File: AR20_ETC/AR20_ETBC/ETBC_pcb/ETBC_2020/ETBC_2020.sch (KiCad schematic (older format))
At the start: 3 parts

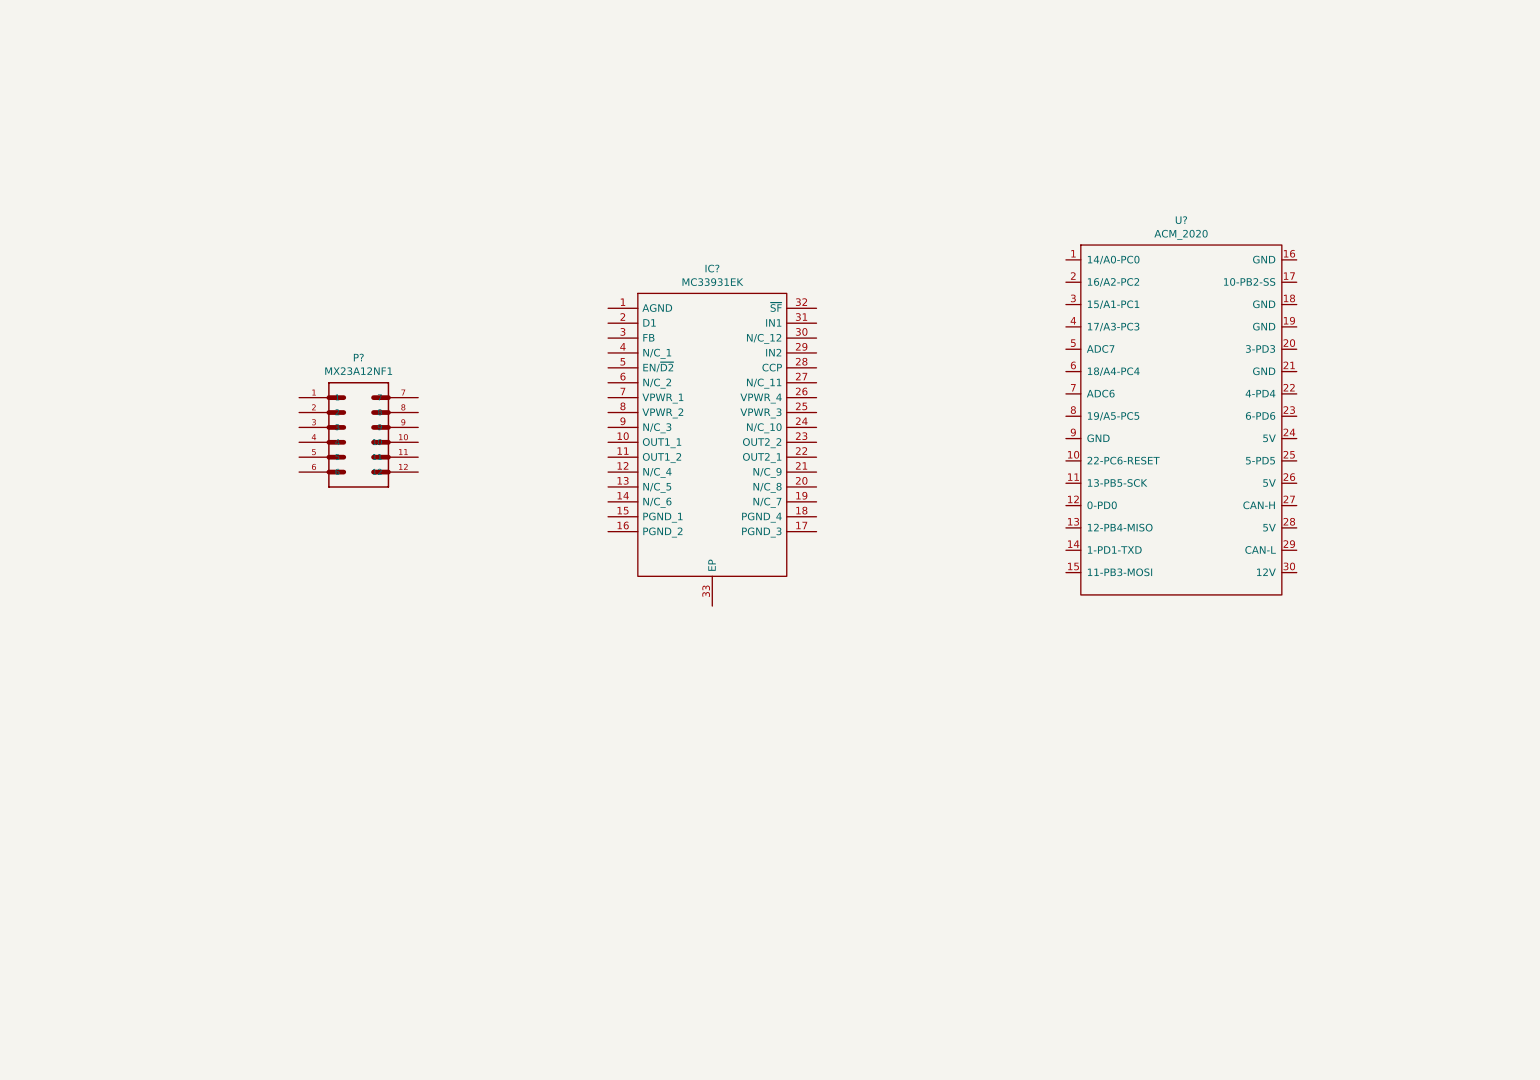
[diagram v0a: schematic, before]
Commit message: Shematic
Added leds
Added small components
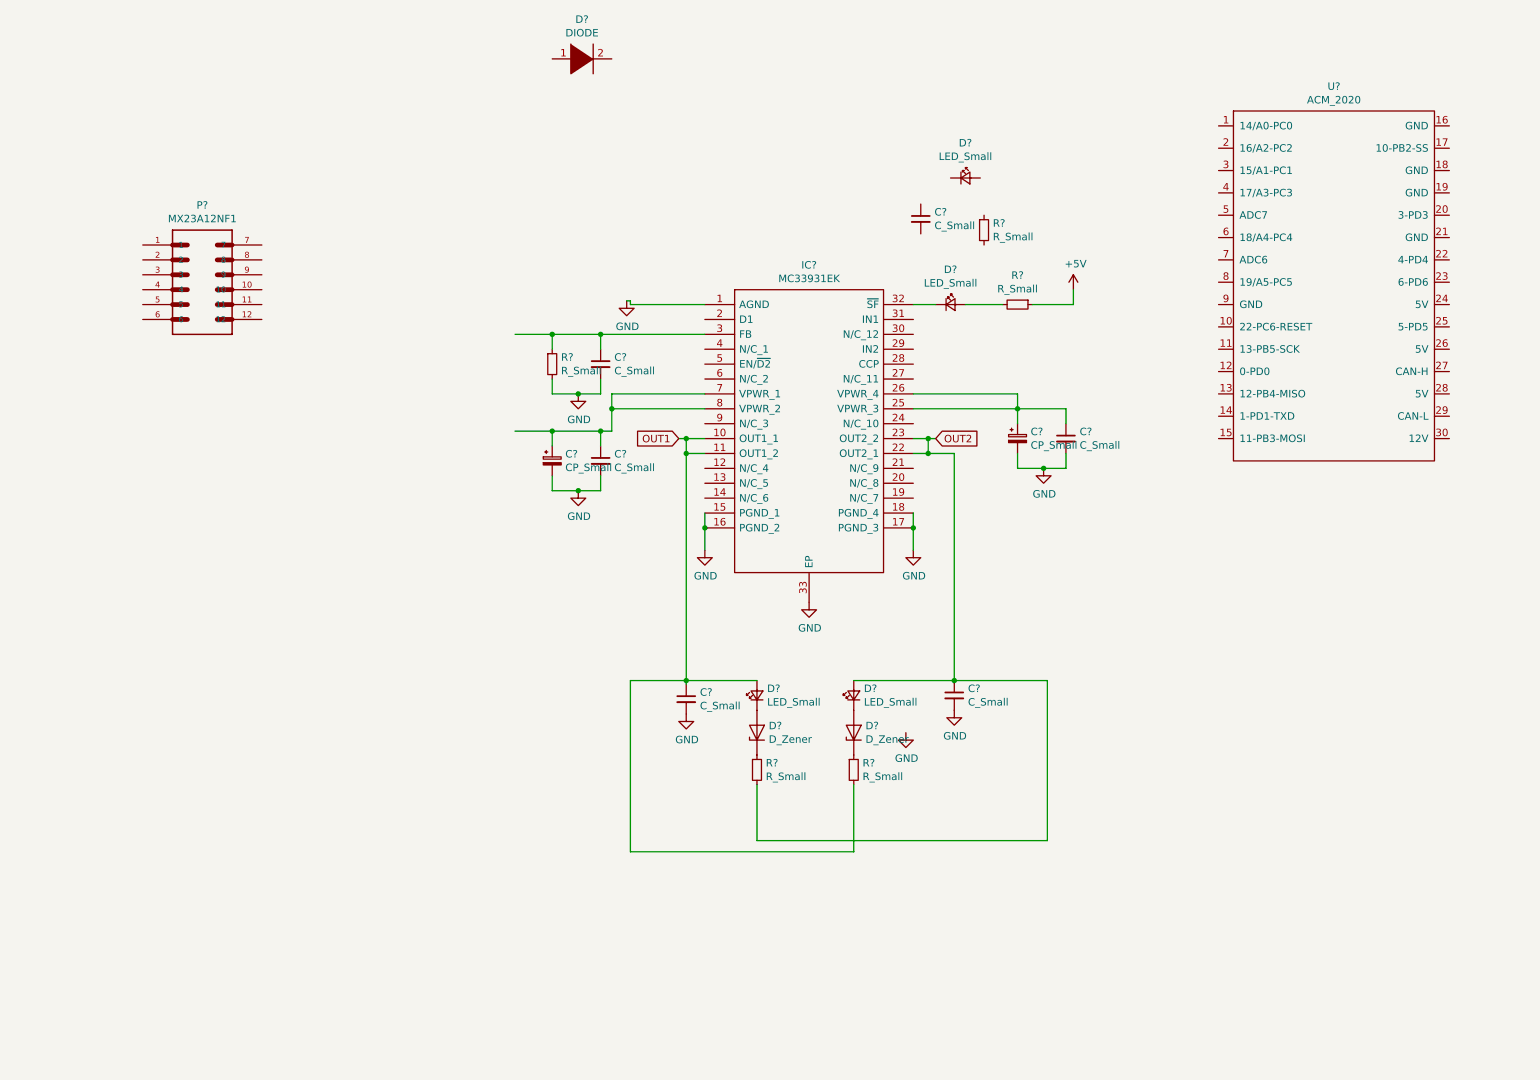
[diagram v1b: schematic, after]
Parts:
- added C? (x6): C_Small, symbol Device:C_Small
- added C? (x2): CP_Small, symbol Device:CP_Small
- added D? (x2): D_Zener, symbol Device:D_Zener
- added D?: DIODE, symbol pspice:DIODE
- added D? (x4): LED_Small, symbol Device:LED_Small
- added R? (x5): R_Small, symbol Device:R_Small
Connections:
- net labels added: +5V, GND, OUT1, OUT2
- wire segments 0 -> 65
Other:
- moved on the sheet: IC?, P?, U?

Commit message: Added filters
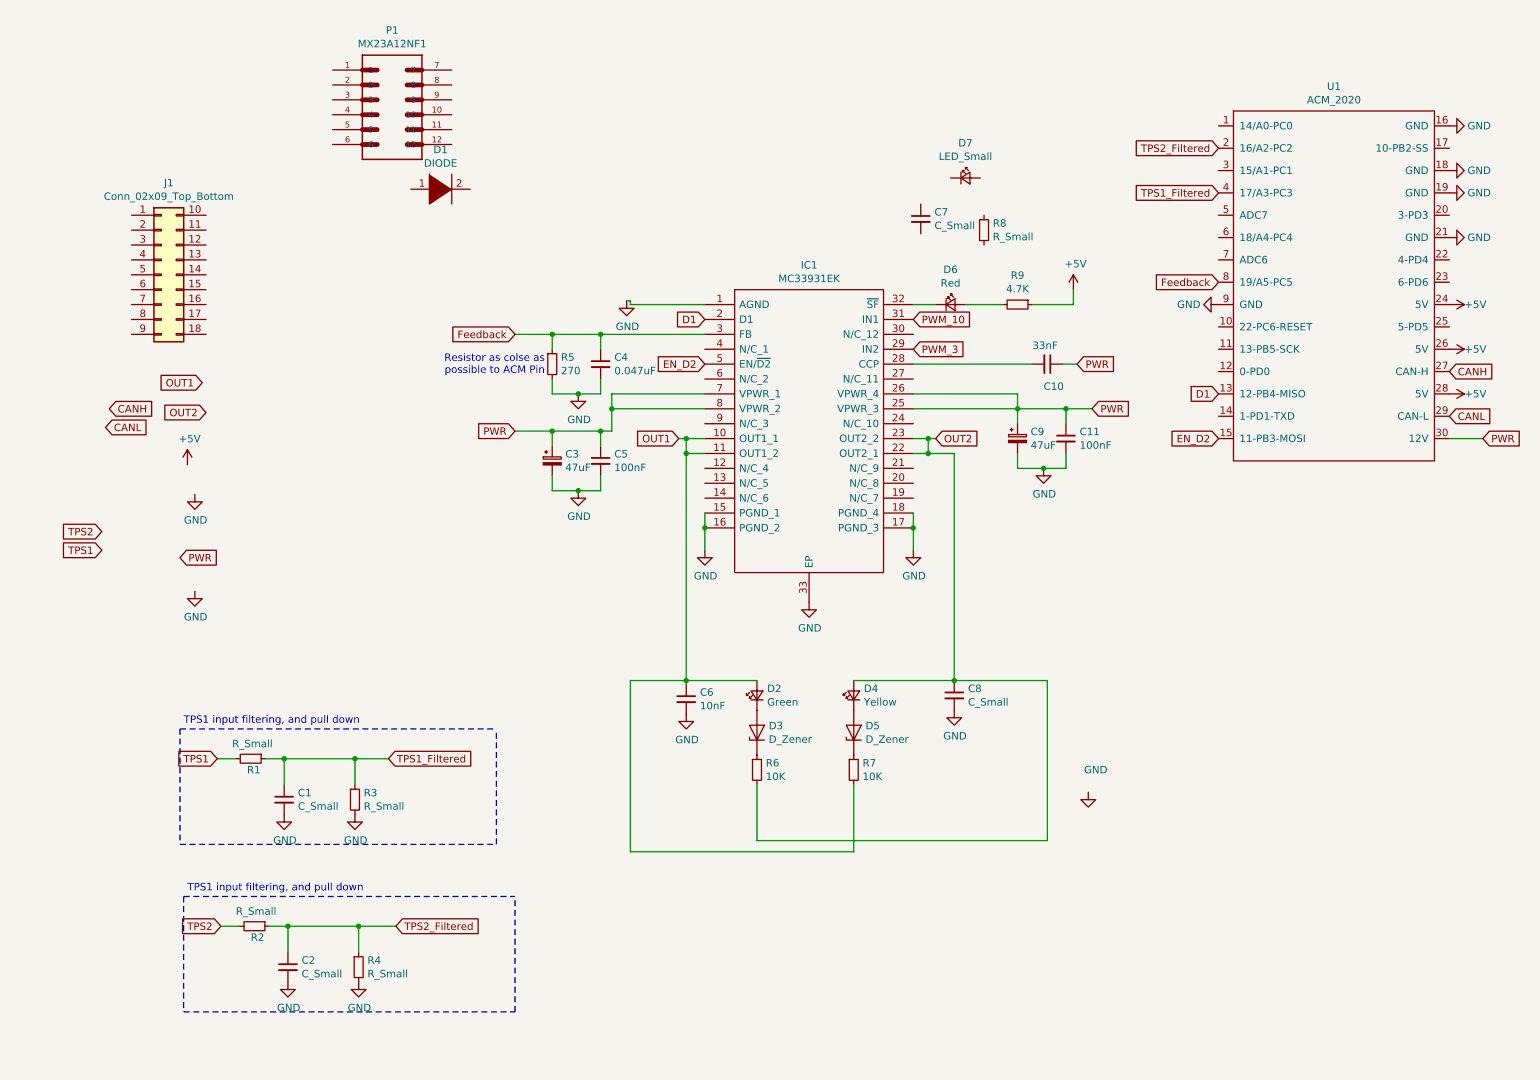
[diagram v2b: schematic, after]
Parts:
- added C1, C2: C_Small, Capacitor_SMD:C_0603_1608Metric_Pad1.05x0.95mm_HandSolder, symbol Device:C_Small
- added C10: 33nF, Capacitor_SMD:C_0603_1608Metric_Pad1.05x0.95mm_HandSolder, symbol Device:C_Small
- added J1: Conn_02x09_Top_Bottom, symbol Connector_Generic:Conn_02x09_Top_Bottom
- added R1, R2, R3, R4: R_Small, Resistor_SMD:R_0603_1608Metric_Pad1.05x0.95mm_HandSolder, symbol Device:R_Small
- C11, C5: renamed from C?; value C_Small -> 100nF; footprint (none) -> Capacitor_SMD:C_0603_1608Metric_Pad1.05x0.95mm_HandSolder
- C3, C9: renamed from C?; value CP_Small -> 47uF; footprint (none) -> Capacitor_SMD:C_0603_1608Metric_Pad1.05x0.95mm_HandSolder
- C4: renamed from C?; value C_Small -> 0.047uF; footprint (none) -> Capacitor_SMD:C_0603_1608Metric_Pad1.05x0.95mm_HandSolder
- C6: renamed from C?; value C_Small -> 10nF; footprint (none) -> Capacitor_SMD:C_0603_1608Metric_Pad1.05x0.95mm_HandSolder
- C7, C8: renamed from C?; footprint (none) -> Capacitor_SMD:C_0603_1608Metric_Pad1.05x0.95mm_HandSolder
- D2: renamed from D?; value LED_Small -> Green
- D4: renamed from D?; value LED_Small -> Yellow
- D6: renamed from D?; value LED_Small -> Red
- R5: renamed from R?; value R_Small -> 270; footprint (none) -> Resistor_SMD:R_0603_1608Metric_Pad1.05x0.95mm_HandSolder
- R6, R7: renamed from R?; value R_Small -> 10K; footprint (none) -> Resistor_SMD:R_0603_1608Metric_Pad1.05x0.95mm_HandSolder
- R8: renamed from R?; footprint (none) -> Resistor_SMD:R_0603_1608Metric_Pad1.05x0.95mm_HandSolder
- R9: renamed from R?; value R_Small -> 4.7K; footprint (none) -> Resistor_SMD:R_0603_1608Metric_Pad1.05x0.95mm_HandSolder
- gave numbers to parts that had none: 7
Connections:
- net labels added: CANH, CANL, D1, EN_D2, Feedback, PWM_10, PWM_3, PWR, TPS1, TPS1_Filtered, TPS2, TPS2_Filtered
- wire segments 65 -> 81
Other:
- note added: "Resistor as colse as\npossible to ACM Pin"
- note added: "TPS1 input filtering, and pull down"
- moved on the sheet: D1, P1
